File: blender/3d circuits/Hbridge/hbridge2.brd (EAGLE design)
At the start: 13 parts, among them Q2 IRLML0060, Q3 IRLML0060, Q4 IRLML0060, Q5 IRLML0060

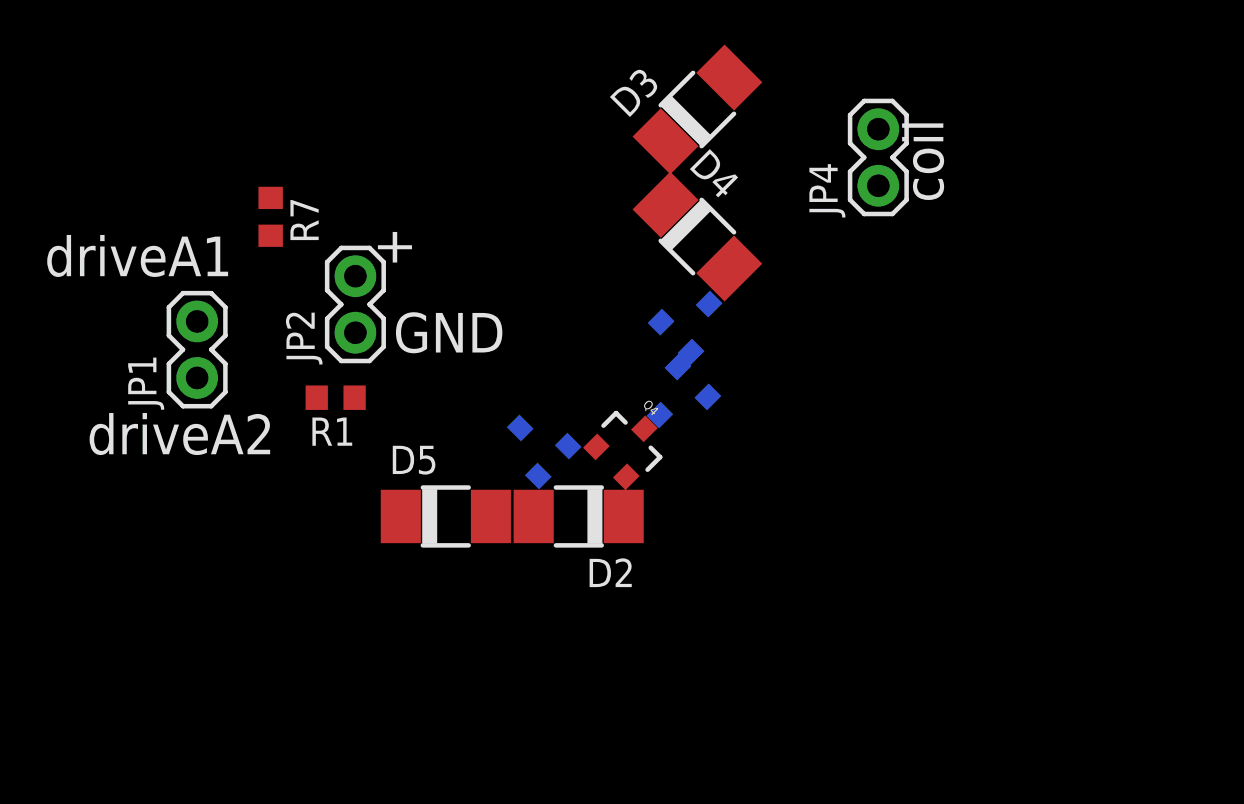
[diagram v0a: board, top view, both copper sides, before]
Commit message: another version of 3d h bridge, better layout
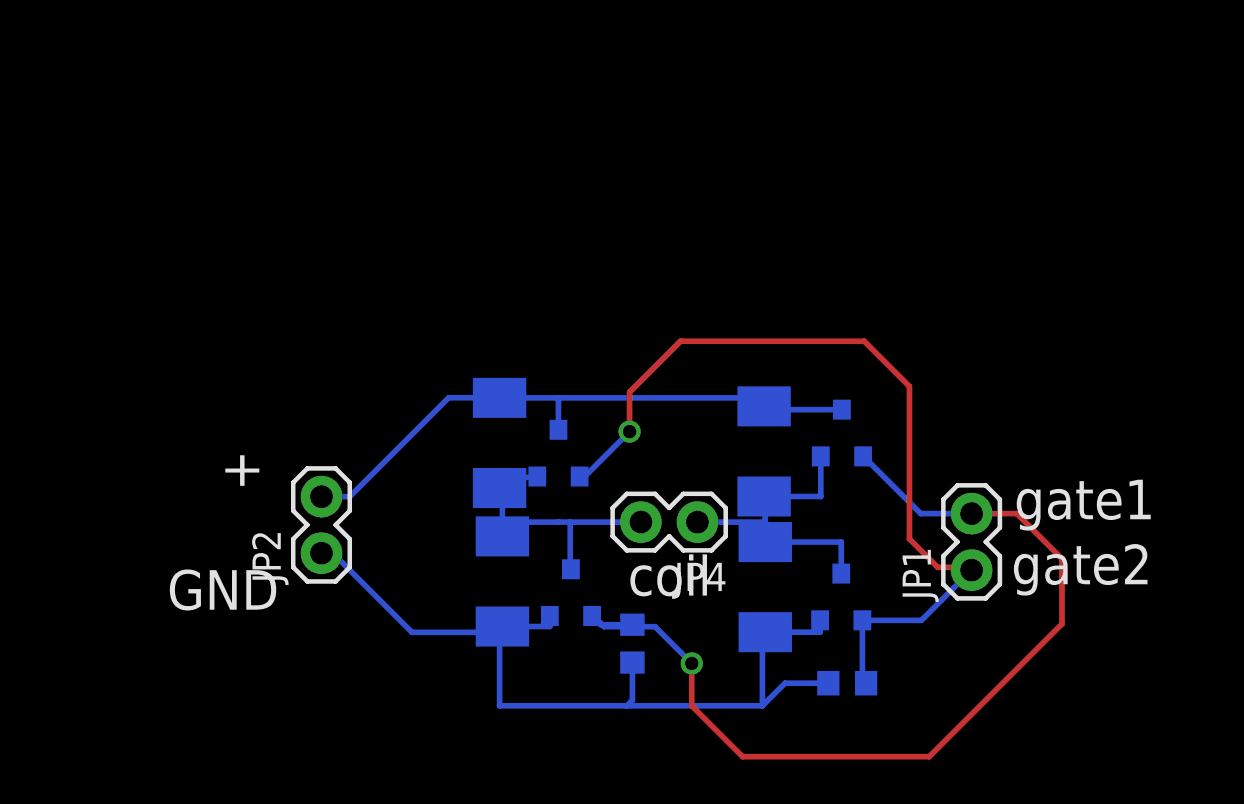
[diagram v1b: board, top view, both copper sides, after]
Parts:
- moved JP1 35.9 mm to (89.5, 14.1)
- moved R1 26.3 mm to (83.9, 9.02), flipped to the bottom
- moved R7 25.1 mm to (74.3, 10.8), flipped to the bottom, turned to 90 degrees
- moved D3 17.4 mm to (68.3, 19.8), flipped to the bottom, turned to 270 degrees
- moved JP4 17.2 mm to (77.2, 16.3), turned to 180 degrees
- moved Q2 14.1 mm to (83.7, 12.8), turned to 0 degrees
- moved D4 10.1 mm to (80.2, 19.4), flipped to the bottom, turned to 270 degrees
- moved JP2 10.0 mm to (60.3, 14.9)
- moved Q4 9.67 mm to (83.7, 20.2), flipped to the bottom, turned to 0 degrees
- moved D2 8.96 mm to (80.3, 13.3), flipped to the bottom, turned to 270 degrees
- moved Q5 6.84 mm to (71.5, 13.0), turned to 0 degrees
- moved Q3 5.91 mm to (71.0, 19.3), turned to 0 degrees
- moved D5 3.87 mm to (68.5, 13.6), flipped to the bottom, turned to 270 degrees
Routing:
- net GATEA1: track 0.00 -> 43.1 mm, vias 0 -> 1
- net GND: track 0.00 -> 39.7 mm
- net GATEA2: track 0.00 -> 38.2 mm, vias 0 -> 1
- net VCC: track 0.00 -> 27.3 mm
- net COILA1: track 0.00 -> 14.3 mm
- net COILA2: track 0.00 -> 12.6 mm
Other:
- board text added: "gate1"
- board text added: "gate2"
- board text removed: "driveA1"
- board text removed: "driveA2"
